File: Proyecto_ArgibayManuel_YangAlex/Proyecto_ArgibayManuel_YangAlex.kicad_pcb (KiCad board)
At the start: 2 copper layers, 130.5 x 67.5 mm, 72 parts, among them IC1 LM1117, J1 Conn_01x02, J10 Con_1x2, J11 Con_1x2, J12 Con_ICSP, J2 Conn_01x01, J3 Con_1x2, J4 Con_1x2, J5 Con_1x2, J6 Con_1x2, J7 Conn_01x03, J8 Conn_01x03, J9 Conn_01x03_Pin, K1 RT314012, K2 RT314012, Q1 2N2222, Q2 2N2222, SW1 SW_Push, SW2 SW_Push, SW3 SW_Push, SW4 SW_Push, U1 PIC18F258-I_SO, U2 HDC2010YPAR, U3 LT1716IS5TRMPBF, U4 LT1716IS5TRMPBF, U5 TXS0108EPW, U6 DRV8871DDA, U7 DRV8871DDA, U8 MCP2551-I-P, X1 DB9, X2 DB9, Y1 Crystal

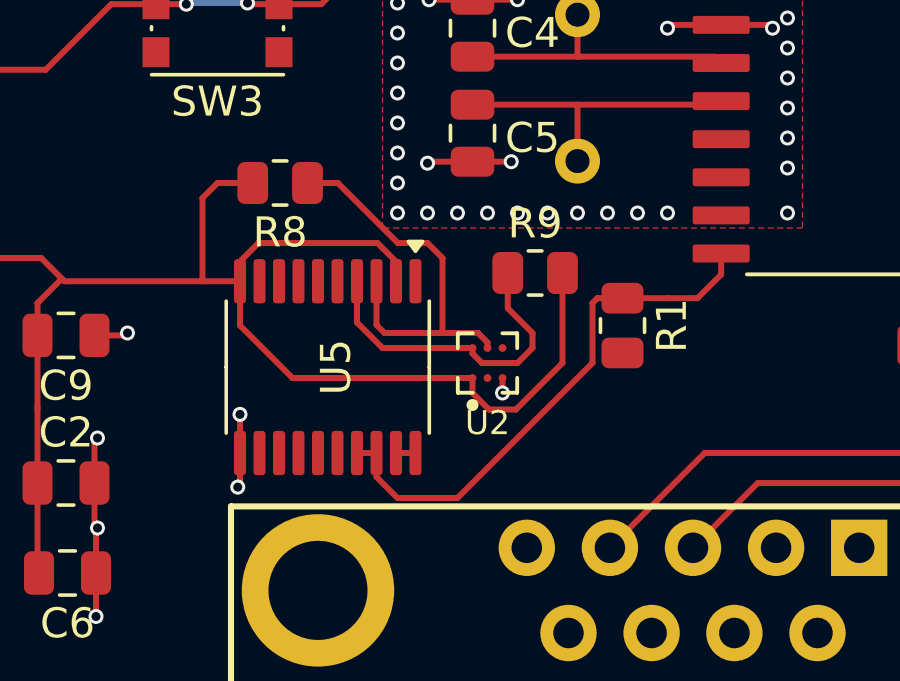
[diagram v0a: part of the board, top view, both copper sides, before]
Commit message: traductor bidireccional(layout)
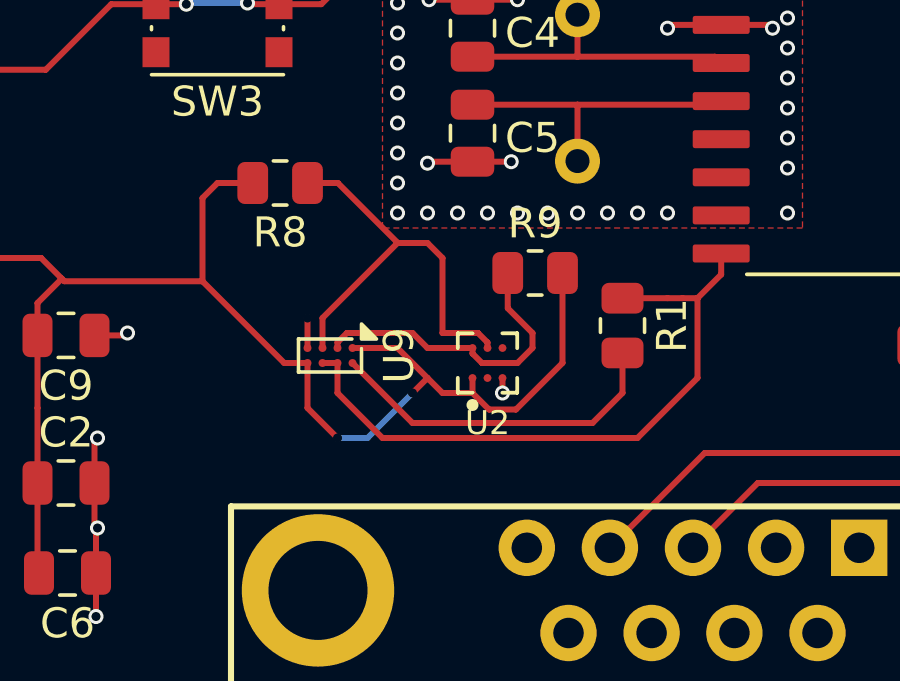
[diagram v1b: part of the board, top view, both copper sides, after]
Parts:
- removed U5: TXS0108EPW, Package_SO:TSSOP-20_4.4x6.5mm_P0.65mm
- added U9: SN74LVC2T45YZP, Package_BGA:Texas_DSBGA-8_0.9x1.9mm_Layout2x4_P0.5mm, F.Cu at (116.2, 80.2)
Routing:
- net VCC: track 0.65 -> 11.6 mm
- net SCL_5V: track 18.2 -> 21.9 mm
- net +3.3V: track 53.2 -> 51.0 mm, vias 0 -> 2
- net GND: track 60.3 -> 58.7 mm, vias 75 -> 74
- net SCL_3,3V: track 13.1 -> 13.9 mm
- net SDA_3,3V: track 10.9 -> 10.4 mm

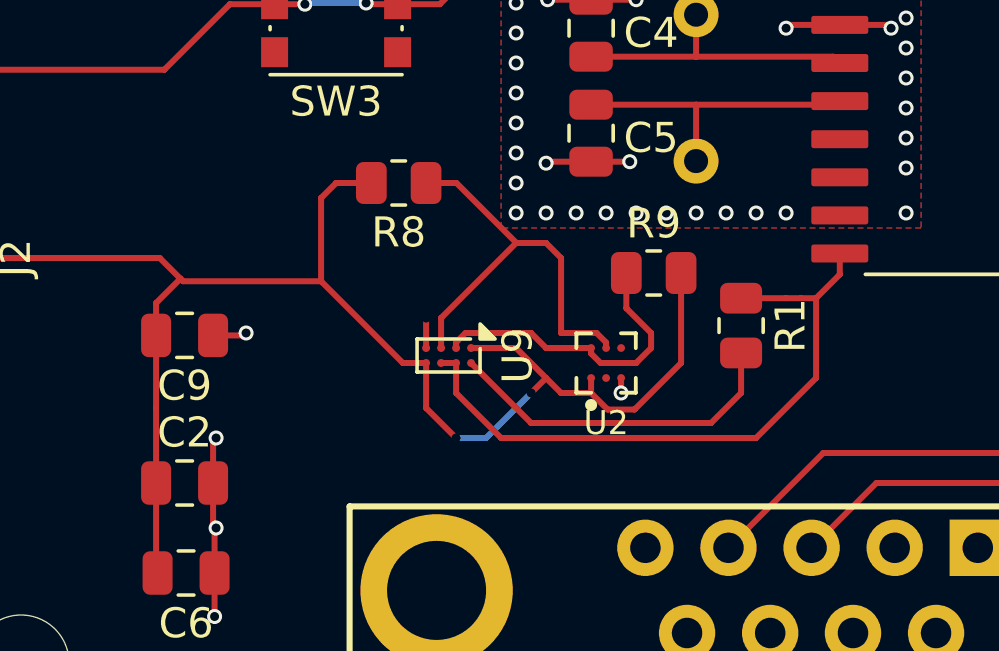
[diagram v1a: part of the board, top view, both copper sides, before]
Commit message: Cambiamos traductor bidireccional
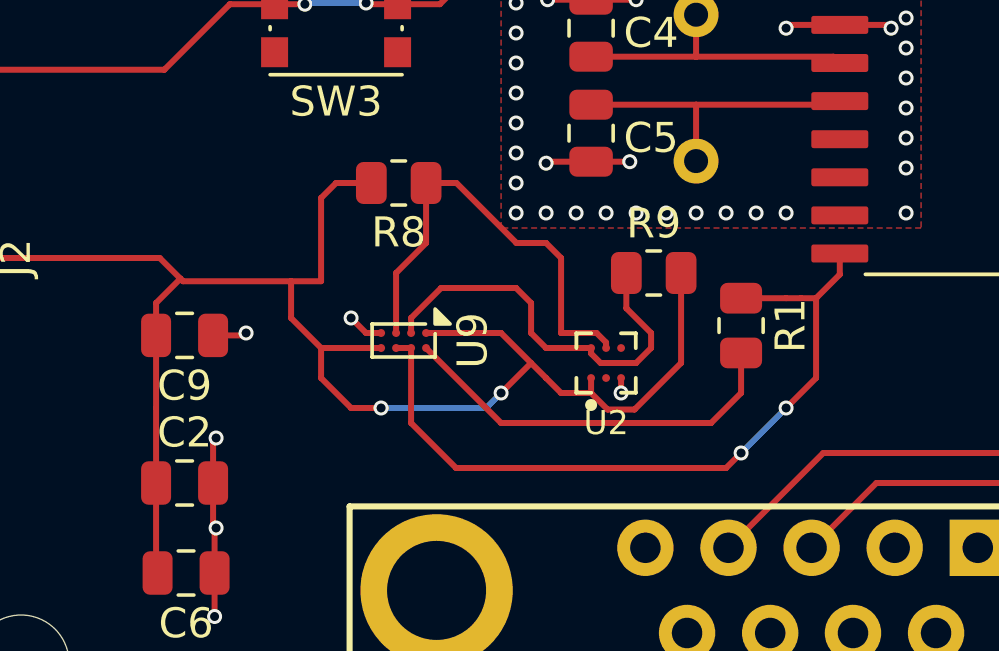
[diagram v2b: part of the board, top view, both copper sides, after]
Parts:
- moved U9 1.58 mm to (114.8, 79.8)
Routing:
- net +3.3V: track 51.0 -> 55.0 mm
- net SCL_5V: track 21.9 -> 25.3 mm, vias 0 -> 2
- net SDA_3,3V: track 10.4 -> 13.7 mm
- net VCC: track 11.6 -> 13.3 mm
- net SCL_3,3V: track 13.9 -> 14.8 mm

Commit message: final
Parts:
- Y1: moved to F.Cu
